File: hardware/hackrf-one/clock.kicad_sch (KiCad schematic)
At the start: 51 parts, among them P1 AD_CLK, P16 CLKIN, P2 CLKOUT, P21 MIX_CLK, P37 SCL, P38 SDA, P57 XCVR_CLK, P59 GCK2, P60 SGPIO_CLK, P72 GP_CLKIN, P8 FSX2_CLK, U16 74LVC1G3157, U19 Si5351A-B-GT, U22 74LVC1G80, U26 74AUP2G58GU, U27 74AUP2G58GU, U28 74AUP2G58GU, X1 GSG-XTAL4PIN

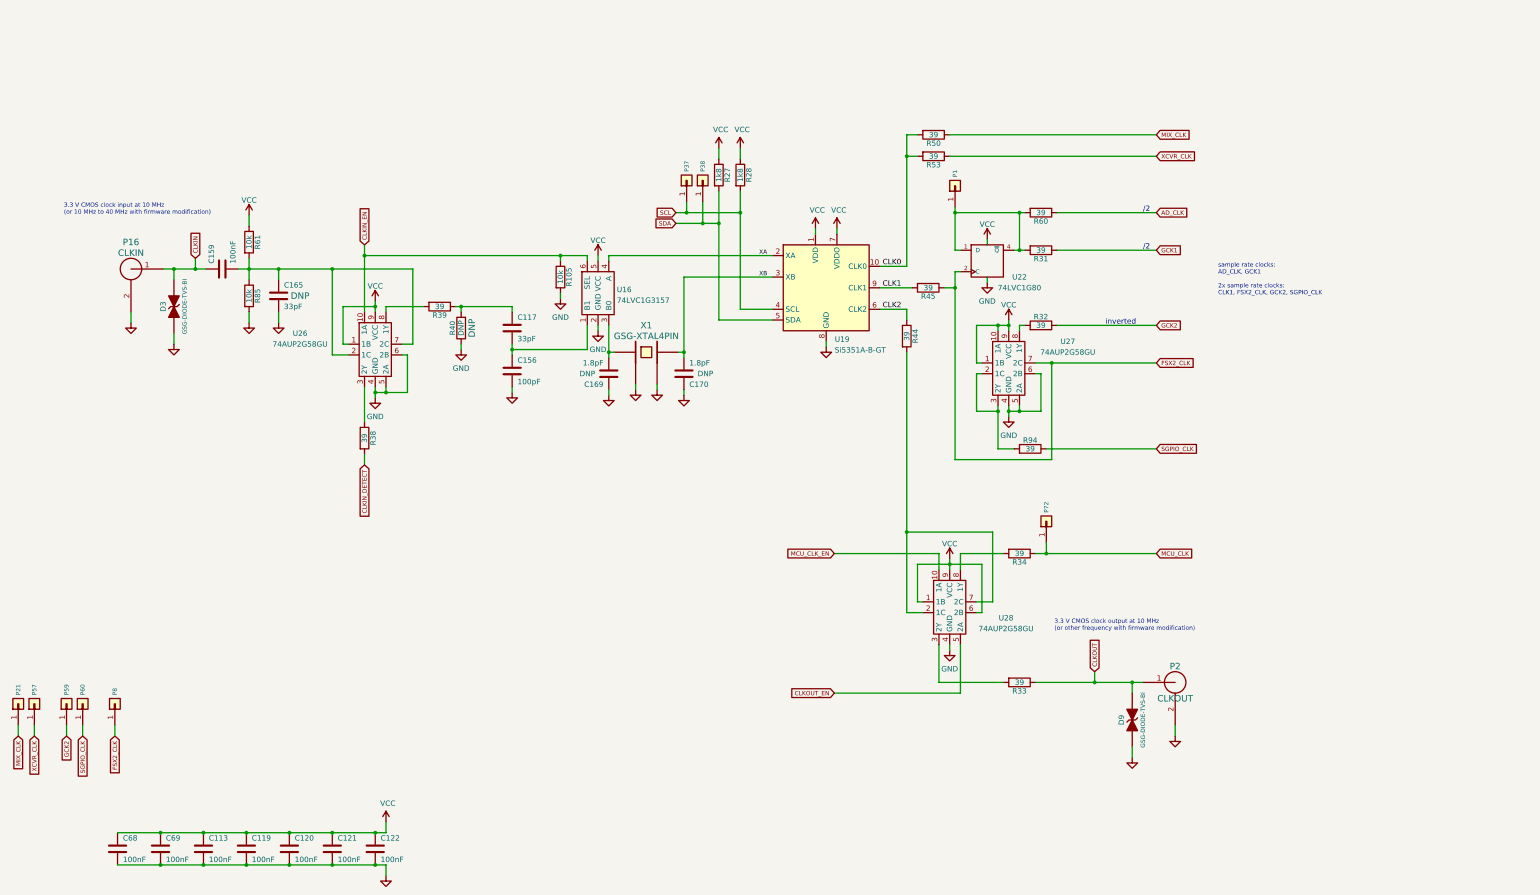
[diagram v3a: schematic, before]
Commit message: HackRF One: add sample clock distribution options
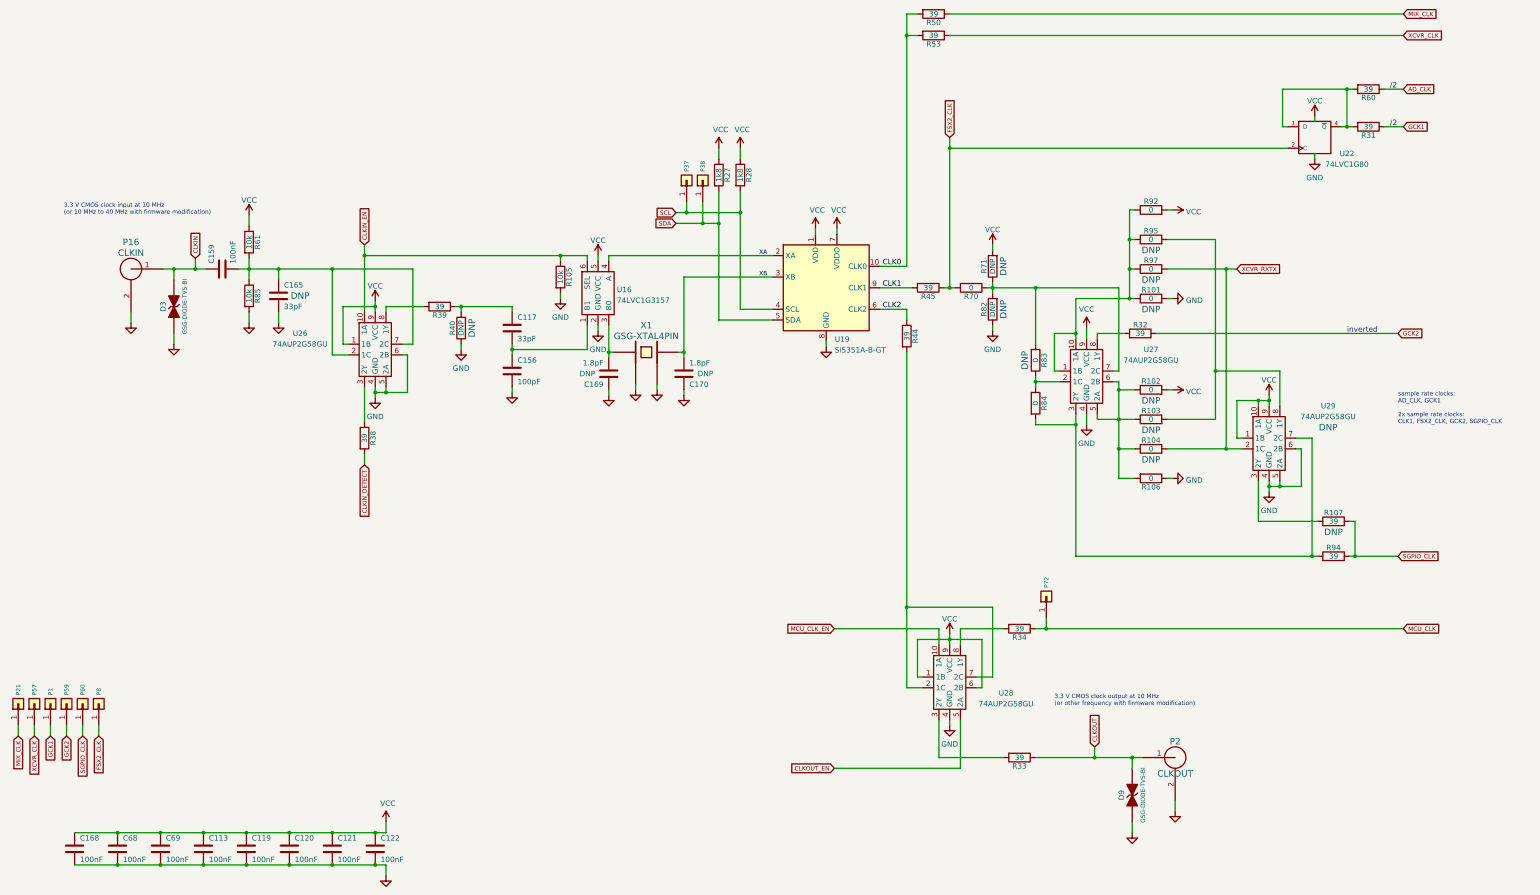
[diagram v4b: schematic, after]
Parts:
- added C168: 100nF, hackrf:GSG-0402, symbol Device:C
- added R101, R102, R103, R104, R106, R70, R83, R84, R92, R95, R97: 0, hackrf:GSG-0402, symbol Device:R
- added R107: 39, hackrf:GSG-0402, symbol Device:R
- added R71, R82: DNP, hackrf:GSG-0402, symbol Device:R
- added U29: 74AUP2G58GU, gsg-modules:XQFN10, symbol 74AUP2G58GU:74AUP2G58GU
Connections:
- net FSX2_CLK: now also R70.2; no longer U27.7 (2C)
- net GCK1: now also P1.1 (Pin_1)
- net GND: now also C168.2, R101.2, R106.1, R82.1, U29.4 (GND), U29.5 (2A), U29.6 (2B); no longer U27.5 (2A), U27.6 (2B)
- net SGPIO_CLK: now also R107.1
- net VCC: now also C168.1, R102.2, R71.2, R92.2, U29.1 (1B), U29.10 (1A), U29.9 (VCC); no longer U27.1 (1B), U27.10 (1A)
- net at R94.2, U27.3 (2Y): now also R84.2, U29.7 (2C); no longer U27.2 (1C)
- net at R31.2, R60.2, U22.1 (D)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: no longer P1.1 (Pin_1)
- new net: R101.1, R92.1, R95.1, R97.1, U27.1 (1B), U27.10 (1A)
- new net: R103.2, R95.2, U29.8 (1Y)
- new net: R70.1, R71.1, R82.2, R83.2, U27.7 (2C)
- new net: R102.1, R103.1, R104.1, R106.2, U27.5 (2A), U27.6 (2B)
- new net: R83.1, R84.1, U27.2 (1C)
- new net: R107.2, U29.3 (2Y)
- new net XCVR_RXTX: R104.2, R97.2, U29.2 (1C)
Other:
- moved on the sheet: D9, P1, P2, P72, P8, R31, R32, R33, R34, R50, R53, R60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
